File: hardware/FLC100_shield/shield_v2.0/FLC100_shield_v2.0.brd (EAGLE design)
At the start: 99.1 x 78.7 mm, 70 parts, among them IC1 TSR 1-2450, IC4 MCP1640, J1 RJ11-6PTH, Q1 2N7000, Q2 2N7000, Q3 2N7000, Q4 2N7000, Q5 2N7000, Q6 2N7000, Q7 2N7000, Q8 2N7000, Q9 2N7000, X1 RJ45, X2 CLOUD SENSOR, X4 HUMIDITY

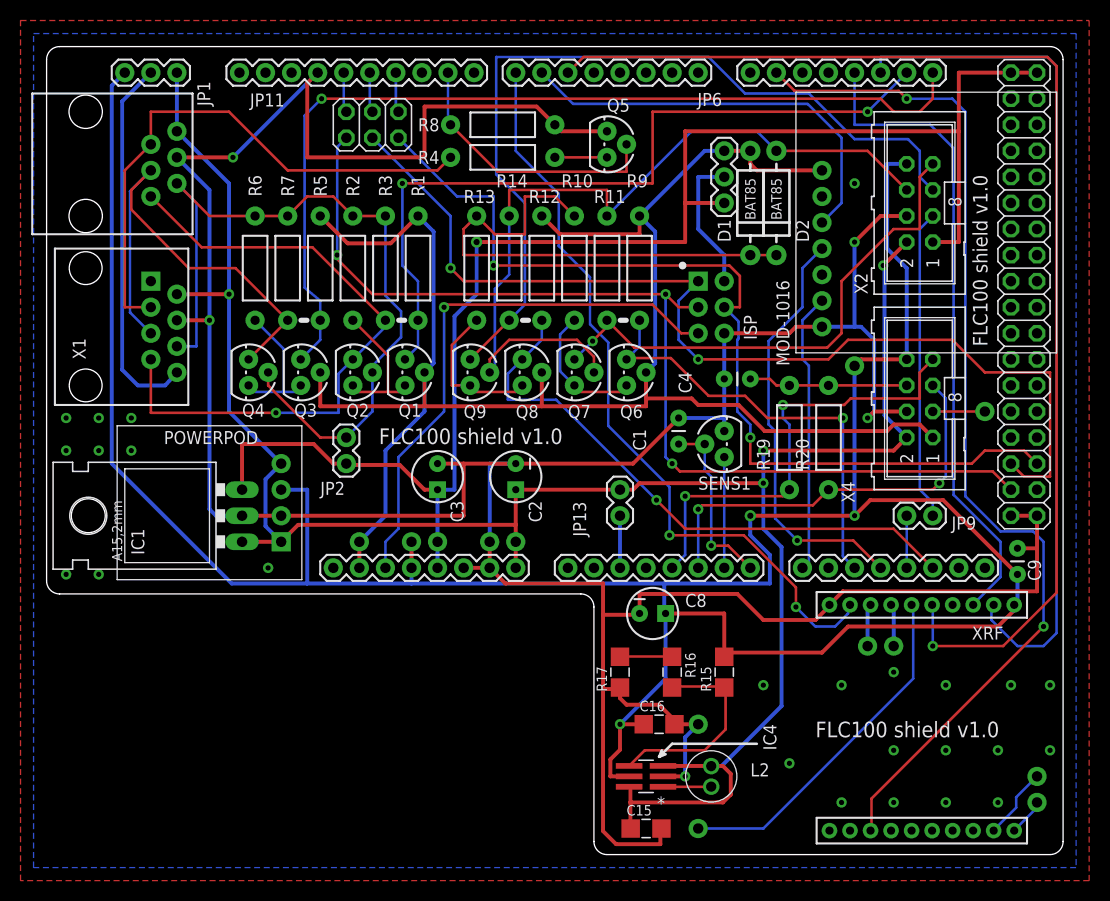
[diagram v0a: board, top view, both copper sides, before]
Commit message: Change footprint for Vin capacitor to ensure 25V rating can be achieved.
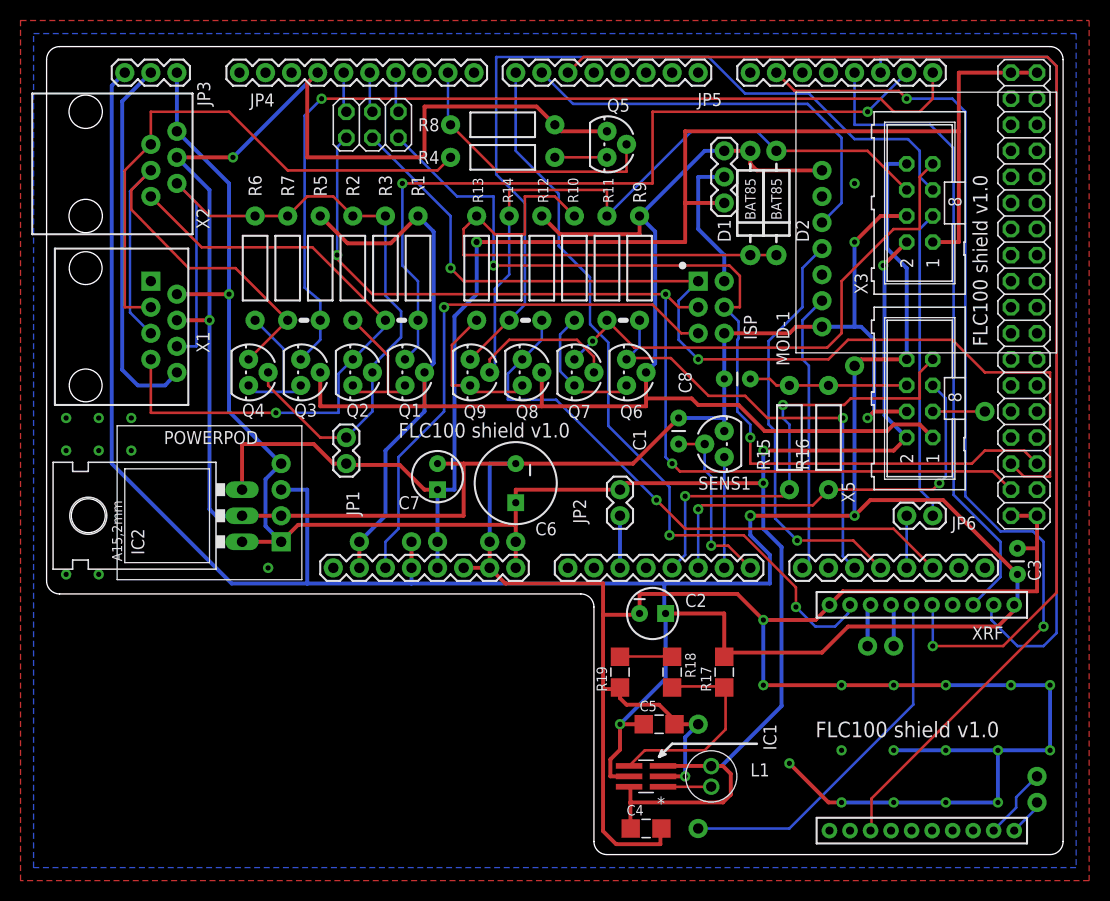
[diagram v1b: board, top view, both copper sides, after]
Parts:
- removed C15: 4u7, SteveMarple:1206-HAND
- removed C9: 100n, SparkFun:CAP-PTH-SMALL
- removed IC4: MCP1640, SteveMarple:SOT23-6-HAND
- removed J1: RJ11-6PTH, SparkFun:RJ11-6
- removed JP13: VIN ADC, SparkFun:1X02
- removed JP9: CLOUD CTRL, SparkFun:1X02
- removed R20: 10k, SteveMarple:RES-AXIAL-0.4
- removed U$16, U$22: PAD, SteveMarple:PAD
- added C6: 4u7 25V, SteveMarple:CPOL-RADIAL-100UF-25V-150MIL
- added C7: 4u7, SteveMarple:CPOL-RADIAL-10UF-25V
- added IC2: TSR 1-2450, SteveMarple:78XXL
- added JP3: MAG VCC, SparkFun:1X03
- added JP5: ISP VCC, SparkFun:1X03
- added R18: 15k, SteveMarple:1206-HAND
- added U$10, U$11: PAD, SteveMarple:PAD
- added X5: HUMIDITY, SteveMarple:ML8
- C2: value 4u7 25V -> 100u; device SparkFun:CPOL-RADIAL-10UF-25V -> SteveMarple:CPOL-RADIAL-10UF-25V
- C3: value 4u7 -> 100n; device SparkFun:CPOL-RADIAL-10UF-25V -> SparkFun:CAP-PTH-SMALL
- C4: value 100n -> 4u7; device SparkFun:CAP-PTH-SMALL -> SteveMarple:1206-HAND
- C8: value 100u -> 100n; device SparkFun:CPOL-RADIAL-10UF-25V -> SparkFun:CAP-PTH-SMALL
- IC1: value TSR 1-2450 -> MCP1640; device SteveMarple:78XXL -> SteveMarple:SOT23-6-HAND
- JP1: value MAG VCC -> 5V LINK; device SparkFun:1X03 -> SparkFun:1X02
- JP2: value 5V LINK -> VIN ADC
- JP6: value ISP VCC -> CLOUD CTRL; device SparkFun:1X03 -> SparkFun:1X02
- R15: value 910k -> 10k; device SteveMarple:1206-HAND -> SteveMarple:RES-AXIAL-0.4
- R16: value 15k -> 10k; device SteveMarple:1206-HAND -> SteveMarple:RES-AXIAL-0.4
- R17: value 510k -> 910k
- R19: value 10k -> 510k; device SteveMarple:RES-AXIAL-0.4 -> SteveMarple:1206-HAND
- U$13: value CALUNIUM-SHIELD-V3 -> PAD; device SteveMarple:CALUNIUM-SHIELD-NO-OUTLINE-NO-HOLES-NO-TEXT-V3 -> SteveMarple:PAD
- U$4: value PAD -> CALUNIUM-SHIELD-V3; device SteveMarple:PAD -> SteveMarple:CALUNIUM-SHIELD-NO-OUTLINE-NO-HOLES-NO-TEXT-V3
- X2: value CLOUD SENSOR -> RJ11; device SteveMarple:ML8 -> SteveMarple:RJ11-6
- X3: value (none) -> CLOUD SENSOR; device pinhead:2X18 -> SteveMarple:ML8
- X4: value HUMIDITY -> MEGA2560; device SteveMarple:ML8 -> pinhead:2X18
- moved X2 81.8 mm to (3.81, 72.4), turned to 270 degrees
- moved U$5 62.3 mm to (30.5, 30.5)
- moved C3 57.3 mm to (94.6, 27.3), turned to 90 degrees
- moved IC1 50.1 mm to (58.4, 7.62), turned to 180 degrees
- moved U$6 46.5 mm to (78.7, 47.6)
- moved U$2 45.6 mm to (38.1, 30.5), turned to 0 degrees
- moved C4 45.0 mm to (58.4, 2.54), turned to 0 degrees
- moved JP1 41.5 mm to (29.2, 38.1), turned to 90 degrees
- moved JP6 39.8 mm to (83.8, 33.0), turned to 0 degrees
- moved U$4 38.1 mm to (63.5, 54.6)
- moved U$13 30.2 mm to (91.4, 43.2)
- moved R19 28.2 mm to (55.9, 17.8)
- moved R16 27.5 mm to (76.2, 40.6), turned to 90 degrees
- moved JP2 26.8 mm to (55.9, 35.6), turned to 270 degrees
- moved C8 24.8 mm to (68.6, 46.4), turned to 180 degrees
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- renumbered C16 to C5, JP11 to JP4, L2 to L1, MOD-1016 to MOD-1, U$23 to U$7, U$25 to U$8, U$32 to U$9, U$40 to U$12
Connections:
- net !RESET: now also U$4.!ISP_RESET, U$4.!RESET@0; no longer U$13.!ISP_RESET, U$13.!RESET@0
- net !XRF_RESET: now also U$4.5; no longer U$13.5
- net +3V3: now also C2.1, C3.1, IC1.5, JP3.3, R17.2, U$3.1, U$4.3.3V, X3.8, X5.8; no longer C8.1, C9.1, IC4.5, JP1.3, R15.2, U$13.3.3V, U$22.1, X2.8, X4.8
- net +5V: now also C7.1, IC2.OUT, JP1.1, JP5.3, U$2.1, U$4.5V, X4.1, X4.2; no longer C3.1, IC1.OUT, JP2.1, JP6.3, U$13.5V, U$3.1, X2.1, X3.2
- net 11: now also U$4.11@0; no longer U$13.11@0
- net 12: now also U$4.12@0; no longer U$13.12@0
- net 13: now also U$4.13@0; no longer U$13.13@0
- net 14: now also U$4.14; no longer U$13.14
- net 16: now also U$4.16; no longer U$13.16
- net 17: now also U$4.17; no longer U$13.17
- net 18: now also JP6.1, U$4.18; no longer JP9.1, U$13.18
- net 19: now also U$4.19; no longer U$13.19
- net 6: now also U$4.6; no longer U$13.6
- net A6: now also U$4.A6; no longer U$13.A6
- net A7: now also U$4.A7; no longer U$13.A7
- net CLOUD_SCL: now also X3.5; no longer X2.5
- net CLOUD_SDA: now also X3.7; no longer X2.7
- net CLOUD_VCC: now also X3.6; no longer X2.6
- net GND: now also C6.2, C7.2, IC1.2, IC2.GND, R19.1, U$14.1, U$4.GND@0, U$4.GND@1, U$4.GND@2, U$4.GND@3, X2.3, X3.4, X4.35, X4.36, X5.4; no longer C15.2, C9.2, IC1.GND, IC4.2, J1.3, R17.1, U$13.GND@0, U$13.GND@1, U$13.GND@2, U$13.GND@3, U$16.1, X2.4, X3.35, X3.36, X4.4
- net HUMIDITY_SCL: now also R16.P$1, U$4.A5/SCL, X5.5; no longer R20.P$1, U$13.A5/SCL, X4.5
- net HUMIDITY_SDA: now also R15.P$1, U$4.A4/SDA, X5.7; no longer R19.P$1, U$13.A4/SDA, X4.7
- net IOREF: now also JP5.1, U$4.IOREF, U$5.1, X5.1; no longer JP6.1, U$13.IOREF, U$14.1, X4.1
- net ISP_VCC: now also JP5.2, U$4.ISP_VCC; no longer JP6.2, U$13.ISP_VCC
- net MAG_SCL: now also X2.4; no longer J1.4
- net MAG_SDA: now also X2.6; no longer J1.6
- net MAG_VCC: now also JP1.2, X2.5; no longer J1.5, JP2.2
- net MISO: now also U$4.ISP_MISO, X4.31; no longer U$13.ISP_MISO, X3.31
- net MOSI: now also U$4.ISP_MOSI, X4.32; no longer U$13.ISP_MOSI, X3.32
- net N$10: now also JP2.2, U$4.A2; no longer JP13.2, U$13.A2
- net N$16: now also U$13.1, X5.3; no longer U$5.1, X4.3
- net N$22: now also C8.1, R15.P$2, R16.P$2, X5.6; no longer C4.1, R19.P$2, R20.P$2, X4.6
- net N$26: now also U$4.9; no longer U$13.9
- net N$3: now also JP6.2, X3.3; no longer JP9.2, X2.3
- net N$41: now also IC1.1; no longer IC4.1
- net N$42: now also R18.1, R19.2; no longer R16.1, R17.2
- net N$46: now also IC1.4, R17.1, R18.2; no longer IC4.4, R15.1, R16.2
- net N$6: now also X2.2; no longer J1.2
- net N$7: now also JP3.2; no longer JP1.2
- net RX1: now also U$4.2@1; no longer U$13.2@1
- net SCK: now also U$4.ISP_SCK, X4.33; no longer U$13.ISP_SCK, X3.33
- net SCL: now also U$4.21@1; no longer U$13.21@1
- net SDA: now also U$4.20@1; no longer U$13.20@1
- net TX1: now also U$4.3@1; no longer U$13.3@1
- net VIN: now also C4.1, C6.1, IC1.3, IC1.6, IC2.IN, JP2.1, JP3.1, U$4.VIN, X2.1, X3.2, X5.2; no longer C15.1, C2.1, IC1.IN, IC4.3, IC4.6, J1.1, JP1.1, JP13.1, U$13.VIN, X2.2, X4.2
- net XRF_ON: now also U$4.23; no longer U$13.23
- net XRF_P1_5: now also U$11.1; no longer U$4.1
- net XRF_P1_6: now also U$10.1; no longer U$2.1
- net XRF_SLEEP: now also U$4.7; no longer U$13.7
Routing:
- net GND: track 347.5 -> 430.3 mm, vias 30 -> 32
- net XRF_HEARTBEAT: track 34.2 -> 35.7 mm

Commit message: Adding extra decoupling for 3.3V.
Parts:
- added C9: 100u, SteveMarple:CPOL-RADIAL-10UF-25V
- C6: value 4u7 25V -> 100u 25V
- moved C6 1.27 mm to (47.0, 36.2)
- moved JP1 1.27 mm to (27.9, 38.1)
- moved C7 1.27 mm to (39.4, 36.8), turned to 90 degrees
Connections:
- net +3V3: now also C9.1
- net GND: now also C9.2
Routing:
- net GND: track 430.3 -> 487.8 mm
- net +3V3: track 270.8 -> 282.1 mm
- net +5V: track 147.9 -> 151.3 mm
- net VIN: track 209.3 -> 208.2 mm

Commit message: Fixing silkscreen and generating Gerber files.
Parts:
- renumbered MOD-1 to MOD1
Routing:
- net GND: track 487.8 -> 489.1 mm
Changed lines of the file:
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@@
 <wire x1="53.34" y1="24.13" x2="53.34" y2="1.27" width="0" layer="20"/>
 <text x="69.215" y="50.165" size="1.27" layer="25" ratio="10" rot="R90">ISP</text>
-<text x="16.51" y="36.83" size="1.016" layer="26" ratio="10" rot="MR0">&gt;DRAWING_NAME</text>
-<text x="16.51" y="34.925" size="1.016" layer="26" ratio="10" rot="MR0">&gt;PLOT_DATE_TIME</text>
+<text x="16.51" y="37.465" size="1.016" layer="26" ratio="10" rot="MR0">&gt;DRAWING_NAME</text>
+<text x="16.51" y="35.56" size="1.016" layer="26" ratio="10" rot="MR0">&gt;PLOT_DATE_TIME</text>
 <text x="96.52" y="11.43" size="1.9304" layer="122" ratio="12" rot="MR0">FLC100 shield v1.0</text>
 <text x="96.52" y="13.97" size="1.016" layer="122" ratio="10" rot="MR0">http://github.com/stevemarple/FLC100_shield</text>
@@
 <wire x1="0" y1="26.67" x2="1.27" y2="25.4" width="0" layer="20" curve="90"/>
 <wire x1="97.79" y1="0" x2="99.06" y2="1.27" width="0" layer="20" curve="90"/>
-<wire x1="24.7904" y1="52.07" x2="25.3746" y2="52.07" width="0.508" layer="112"/>
-<wire x1="34.3154" y1="52.07" x2="34.8996" y2="52.07" width="0.508" layer="112"/>
-<wire x1="46.3804" y1="52.07" x2="46.9646" y2="52.07" width="0.508" layer="112"/>
-<wire x1="55.9054" y1="52.07" x2="56.4896" y2="52.07" width="0.508" layer="112"/>
+<wire x1="24.7904" y1="52.07" x2="25.3746" y2="52.07" width="0.508" layer="121"/>
+<wire x1="34.3154" y1="52.07" x2="34.8996" y2="52.07" width="0.508" layer="121"/>
+<wire x1="46.3804" y1="52.07" x2="46.9646" y2="52.07" width="0.508" layer="121"/>
+<wire x1="55.9054" y1="52.07" x2="56.4896" y2="52.07" width="0.508" layer="121"/>
 <text x="64.516" y="69.215" size="1.27" layer="27" ratio="10" rot="R180">IOREF</text>
 <text x="64.516" y="64.135" size="1.27" layer="27" ratio="10" rot="R180">+5V</text>
@@
 <attribute name="VALUE" x="27.94" y="30.48" size="1.016" layer="27" ratio="10" rot="R90"/>
 </element>
-<element name="X4" library="pinhead" package="2X18" value="MEGA2560" x="95.25" y="54.61" smashed="yes" rot="R270">
-<attribute name="VALUE" x="90.805" y="77.47" size="1.27" layer="27" rot="R270"/>
-</element>
+<element name="X4" library="pinhead" package="2X18" value="MEGA2560" x="95.25" y="54.61" smashed="yes" rot="R270"/>
 <element name="X2" library="SteveMarple" package="RJ11-6" value="RJ11" x="3.81" y="72.39" smashed="yes" rot="R270">
 <attribute name="NAME" x="15.875" y="60.96" size="1.27" layer="25" ratio="10" rot="R90"/>
 <attribute name="VALUE" x="17.78" y="60.96" size="1.27" layer="27" ratio="10" rot="R90"/>
 </element>
-<element name="MOD-1" library="SteveMarple" package="EMBEDDED_ADVENTURES_MOD-1016-NO-HOLES" value="" x="85.725" y="61.595" smashed="yes" rot="R270">
+<element name="MOD1" library="SteveMarple" package="EMBEDDED_ADVENTURES_MOD-1016-NO-HOLES" value="" x="85.725" y="61.595" smashed="yes" rot="R270">
 <attribute name="NAME" x="72.39" y="47.625" size="1.27" layer="25" font="vector" ratio="10" rot="R90"/>
 <attribute name="VALUE" x="83.185" y="64.135" size="1.27" layer="21" font="vector" rot="R270"/>
@@
 <element name="IC2" library="SteveMarple" package="78XXL" value="TSR 1-2450" x="15.24" y="33.02" smashed="yes" rot="R90">
 <attribute name="NAME" x="9.525" y="29.21" size="1.27" layer="25" ratio="10" rot="R90"/>
-<attribute name="VALUE" x="11.43" y="29.083" size="1.016" layer="27" ratio="10" rot="R90"/>
+<attribute name="VALUE" x="11.43" y="28.448" size="1.016" layer="27" ratio="10" rot="R90"/>
 </element>
 <element name="Q6" library="SteveMarple" package="TO-92" value="2N7000" x="56.515" y="46.99" smashed="yes" rot="R270">
@@
 <element name="R17" library="SteveMarple" package="1206-HAND" value="910k" x="66.04" y="17.78" smashed="yes" rot="R90">
 <attribute name="NAME" x="64.77" y="15.875" size="1.016" layer="25" ratio="10" rot="R90"/>
-<attribute name="VALUE" x="68.326" y="15.875" size="1.016" layer="27" rot="R90"/>
+<attribute name="VALUE" x="69.342" y="16.51" size="1.016" layer="27" rot="R90"/>
 </element>
 <element name="R18" library="SteveMarple" package="1206-HAND" value="15k" x="60.96" y="17.78" smashed="yes" rot="R270">
-<attribute name="NAME" x="62.23" y="19.685" size="1.016" layer="25" ratio="10" rot="R270"/>
-<attribute name="VALUE" x="58.674" y="19.685" size="1.016" layer="27" rot="R270"/>
+<attribute name="NAME" x="59.69" y="15.875" size="1.016" layer="25" ratio="10" rot="R90"/>
+<attribute name="VALUE" x="63.246" y="15.875" size="1.016" layer="27" rot="R90"/>
 </element>
 <element name="C5" library="SteveMarple" package="1206-HAND" value="10u" x="59.69" y="12.7" smashed="yes">
@@
 <element name="U$8" library="SteveMarple" package="PAD" value="PAD" x="96.52" y="7.62" smashed="yes"/>
 <element name="C2" library="SteveMarple" package="CPOL-RADIAL-10UF-25V" value="100u" x="59.055" y="23.495" smashed="yes">
-<attribute name="NAME" x="62.23" y="24.13" size="1.27" layer="25" ratio="10"/>
-<attribute name="VALUE" x="62.23" y="22.225" size="1.27" layer="27" ratio="10"/>
+<attribute name="NAME" x="63.119" y="21.59" size="1.27" layer="25" ratio="10" rot="R90"/>
+<attribute name="VALUE" x="64.77" y="20.701" size="1.27" layer="27" ratio="10" rot="R90"/>
 </element>
 <element name="C3" library="SparkFun" package="CAP-PTH-SMALL" value="100n" x="94.615" y="27.305" smashed="yes" rot="R90">
@@
 <element name="U$13" library="SteveMarple" package="PAD" value="PAD" x="91.44" y="43.18" smashed="yes"/>
 <element name="R15" library="SteveMarple" package="RES-AXIAL-0.4" value="10k" x="72.39" y="40.64" smashed="yes" rot="R90">
-<attribute name="NAME" x="70.485" y="37.465" size="1.27" layer="25" font="vector" ratio="10" rot="R90"/>
+<attribute name="NAME" x="72.39" y="31.115" size="1.27" layer="25" font="vector" ratio="10" rot="R90"/>
 <attribute name="VALUE" x="72.39" y="40.64" size="1.27" layer="27" font="vector" ratio="10" rot="R90" align="center"/>
 </element>
 <element name="R16" library="SteveMarple" package="RES-AXIAL-0.4" value="10k" x="76.2" y="40.64" smashed="yes" rot="R90">
-<attribute name="NAME" x="74.295" y="37.465" size="1.27" layer="25" font="vector" ratio="10" rot="R90"/>
+<attribute name="NAME" x="76.2" y="31.115" size="1.27" layer="25" font="vector" ratio="10" rot="R90"/>
 <attribute name="VALUE" x="76.2" y="40.64" size="1.27" layer="27" font="vector" ratio="10" rot="R90" align="center"/>
 </element>
@@
 <element name="U$11" library="SteveMarple" package="PAD" value="PAD" x="80.01" y="20.32"/>
 <element name="D1" library="SteveMarple" package="DIODE-TH-0.4" value="BAT85" x="68.58" y="63.5" smashed="yes" rot="R270">
-<attribute name="NAME" x="66.675" y="59.69" size="1.27" layer="25" ratio="10" rot="R90"/>
+<attribute name="NAME" x="69.215" y="54.61" size="1.27" layer="25" ratio="10" rot="R90"/>
 <attribute name="VALUE" x="69.088" y="61.849" size="1.016" layer="21" ratio="10" rot="R90"/>
 </element>
 <element name="D2" library="SteveMarple" package="DIODE-TH-0.4" value="BAT85" x="71.12" y="63.5" smashed="yes" rot="R270">
-<attribute name="NAME" x="74.295" y="59.69" size="1.27" layer="25" ratio="10" rot="R90"/>
+<attribute name="NAME" x="71.755" y="54.61" size="1.27" layer="25" ratio="10" rot="R90"/>
 <attribute name="VALUE" x="71.628" y="61.849" size="1.016" layer="21" ratio="10" rot="R90"/>
 </element>
@@
 <contactref element="X4" pad="36"/>
 <contactref element="X4" pad="35"/>
-<contactref element="MOD-1" pad="GND"/>
-<contactref element="MOD-1" pad="GND"/>
+<contactref element="MOD1" pad="GND"/>
+<contactref element="MOD1" pad="GND"/>
 <contactref element="IC2" pad="GND"/>
 <contactref element="X2" pad="3"/>
@@
 <via x="82.55" y="16.51" extent="1-16" drill="0.508"/>
 <via x="77.47" y="16.51" extent="1-16" drill="0.508"/>
-<via x="69.85" y="16.51" extent="1-16" drill="0.508"/>
+<via x="69.85" y="15.875" extent="1-16" drill="0.508"/>
 <via x="72.39" y="8.89" extent="1-16" drill="0.508"/>
 <via x="5.08" y="27.305" extent="1-16" drill="0.508"/>
 <via x="69.85" y="22.86" extent="1-16" drill="0.508"/>
-<wire x1="69.85" y1="22.86" x2="69.85" y2="16.51" width="0.381" layer="16"/>
+<wire x1="69.85" y1="22.86" x2="69.85" y2="15.875" width="0.381" layer="16"/>
 <wire x1="77.47" y1="16.51" x2="69.85" y2="16.51" width="0.381" layer="1"/>
+<wire x1="69.85" y1="16.51" x2="69.85" y2="15.875" width="0.381" layer="1"/>
 <wire x1="77.47" y1="16.51" x2="82.55" y2="16.51" width="0.381" layer="1"/>
 <wire x1="82.55" y1="16.51" x2="87.63" y2="16.51" width="0.381" layer="1"/>
@@
 <contactref element="R1" pad="P$2"/>
 <contactref element="Q1" pad="2"/>
-<contactref element="MOD-1" pad="VCC"/>
+<contactref element="MOD1" pad="VCC"/>
 <contactref element="R12" pad="P$2"/>
 <contactref element="Q8" pad="2"/>
@@
 <signal name="6">
 <contactref element="U$4" pad="6"/>
-<contactref element="MOD-1" pad="IRQ"/>
+<contactref element="MOD1" pad="IRQ"/>
 <wire x1="51.308" y1="73.152" x2="48.26" y2="76.2" width="0.254" layer="16"/>
 <wire x1="74.168" y1="73.152" x2="51.308" y2="73.152" width="0.254" layer="16"/>
@@
 <signal name="14">
 <contactref element="U$4" pad="14"/>
-<contactref element="MOD-1" pad="SDA_MOSI"/>
+<contactref element="MOD1" pad="SDA_MOSI"/>
 <wire x1="74.295" y1="28.575" x2="73.66" y2="27.94" width="0.254" layer="16"/>
 <wire x1="74.295" y1="47.625" x2="74.295" y2="28.575" width="0.254" layer="16"/>
@@
 <signal name="17">
 <contactref element="U$4" pad="17"/>
-<contactref element="MOD-1" pad="SCL"/>
+<contactref element="MOD1" pad="SCL"/>
 <wire x1="78.613" y1="30.607" x2="81.28" y2="27.94" width="0.254" layer="1"/>
 <wire x1="73.152" y1="30.607" x2="78.613" y2="30.607" width="0.254" layer="1"/>
